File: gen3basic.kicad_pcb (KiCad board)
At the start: 2 copper layers, 35 parts, among them J1 AVR-ISP-6, J2 Screw_Terminal_01x02, J3 Conn_01x08, J4 Conn_01x08, J5 Conn_01x08, J6 Screw_Terminal_01x04, U1 ATMEGA328-PU, Y1 Resonator

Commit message: moved a bunch of stuff around.
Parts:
- removed REF** (x3): MountingHole_2.2mm_M2_DIN965, MountingHole:MountingHole_2.2mm_M2_DIN965
- removed TP1, TP2, TP3: TestPoint, TestPoint:TestPoint_Pad_1.5x1.5mm
- removed TP4: TestPoint, TestPoint:TestPoint_Pad_1.0x1.0mm
- added C4: 100 nF, Capacitor_SMD:C_0805_2012Metric_Pad1.15x1.40mm_HandSolder, F.Cu at (79.2, 49.3)
- added C7: 22pF, Capacitor_SMD:C_0805_2012Metric_Pad1.15x1.40mm_HandSolder, F.Cu at (63.9, 70.0)
- added C8: 22pF, Capacitor_SMD:C_0805_2012Metric_Pad1.15x1.40mm_HandSolder, F.Cu at (59.9, 65.9)
- added D3: 1N4148WS, Diode_SMD:D_SOD-323, F.Cu at (86.4, 53.6)
- added H1: MountingHole, MountingHole:MountingHole_2.2mm_M2_ISO7380, F.Cu at (54.4, 89.9)
- added H2: MountingHole, MountingHole:MountingHole_2.2mm_M2_ISO7380, F.Cu at (78.2, 57.4)
- added H3: MountingHole, MountingHole:MountingHole_2.2mm_M2_ISO7380, F.Cu at (82.3, 80.8)
- added J5: Conn_01x06, Connector_PinHeader_2.54mm:PinHeader_1x06_P2.54mm_Horizontal, F.Cu at (78.1, 46.4)
- added R3: 10k, Resistor_SMD:R_0805_2012Metric_Pad1.15x1.40mm_HandSolder, F.Cu at (87.1, 49.3)
- added R6: 1M, Resistor_SMD:R_0805_2012Metric_Pad1.15x1.40mm_HandSolder, F.Cu at (62.0, 67.9)
- added R7: 330k, Resistor_SMD:R_0805_2012Metric_Pad1.15x1.40mm_HandSolder, F.Cu at (79.5, 69.1)
- added R8: 330k, Resistor_SMD:R_0805_2012Metric_Pad1.15x1.40mm_HandSolder, F.Cu at (84.1, 71.6)
- added S3: MOMENTARY-SWITCH-SPST-SMD-5.2-REDUNDANT, SparkFun-Switches:TACTILE_SWITCH_SMD_5.2MM, F.Cu at (81.3, 75.4)
- added S4: EG1224, Button_Switch_THT:SW_E-Switch_EG1224_SPDT_Angled, F.Cu at (80.0, 88.6)
- C1: footprint Capacitor_SMD:C_1210_3225Metric_Pad1.42x2.65mm_HandSolder -> Capacitor_SMD:C_0805_2012Metric_Pad1.15x1.40mm_HandSolder
- C3: value C -> 100 nF; footprint Capacitor_SMD:C_1210_3225Metric_Pad1.42x2.65mm_HandSolder -> Capacitor_SMD:C_0805_2012Metric_Pad1.15x1.40mm_HandSolder
- C5: renamed from C4; value C -> 100 nF; footprint Capacitor_SMD:C_1210_3225Metric_Pad1.42x2.65mm_HandSolder -> Capacitor_SMD:C_0805_2012Metric_Pad1.15x1.40mm_HandSolder
- D1: footprint LED_SMD:LED_1210_3225Metric_Pad1.42x2.65mm_HandSolder -> LED_THT:LED_D5.0mm_Clear
- D2: footprint LED_SMD:LED_1210_3225Metric_Pad1.42x2.65mm_HandSolder -> LED_SMD:LED_0805_2012Metric_Pad1.15x1.40mm_HandSolder
- D4: renamed from D3; footprint LED_SMD:LED_1210_3225Metric_Pad1.42x2.65mm_HandSolder -> LED_THT:LED_D5.0mm_Clear
- D5: renamed from D4; footprint LED_SMD:LED_1210_3225Metric_Pad1.42x2.65mm_HandSolder -> LED_THT:LED_D5.0mm_Clear
- J3: value Conn_01x08 -> Conn_01x06; footprint Connector_PinHeader_2.54mm:PinHeader_1x08_P2.54mm_Vertical -> Connector_PinHeader_2.54mm:PinHeader_1x06_P2.54mm_Vertical
- J4: value Conn_01x08 -> Conn_01x07; footprint Connector_PinHeader_2.54mm:PinHeader_1x08_P2.54mm_Vertical -> Connector_PinHeader_2.54mm:PinHeader_1x07_P2.54mm_Vertical
- R1: footprint Resistor_SMD:R_1210_3225Metric_Pad1.42x2.65mm_HandSolder -> Resistor_SMD:R_0805_2012Metric_Pad1.15x1.40mm_HandSolder
- R2: footprint Resistor_SMD:R_1210_3225Metric_Pad1.42x2.65mm_HandSolder -> Resistor_SMD:R_1206_3216Metric_Pad1.42x1.75mm_HandSolder
- R4: renamed from R3; footprint Resistor_SMD:R_1210_3225Metric_Pad1.42x2.65mm_HandSolder -> Resistor_SMD:R_1206_3216Metric_Pad1.42x1.75mm_HandSolder
- R5: renamed from R4; footprint Resistor_SMD:R_1210_3225Metric_Pad1.42x2.65mm_HandSolder -> Resistor_SMD:R_1206_3216Metric_Pad1.42x1.75mm_HandSolder
- S1, S2: value 1825910-6 -> MOMENTARY-SWITCH-SPST-SMD-5.2-REDUNDANT; footprint digikey-footprints:Switch_Tactile_THT_6x6mm -> SparkFun-Switches:TACTILE_SWITCH_SMD_5.2MM
- Y1: value Resonator -> 16.0000MHZ 20PF; footprint Crystal:Resonator-3Pin_W10.0mm_H5.0mm -> Crystal:Crystal_HC49-U_Vertical
- moved C6 17.3 mm to (88.9, 53.3)
- moved J1 12.8 mm to (88.3, 59.1)
- moved C2 12.4 mm to (70.1, 83.6)
- moved D2 8.42 mm to (79.8, 84.1)
- moved R1 7.50 mm to (84.3, 84.1)
- moved C1 7.12 mm to (75.4, 84.1)
- moved R2 5.46 mm to (55.6, 83.1)
- moved S2 5.32 mm to (56.1, 57.4)
- moved S1 5.13 mm to (56.1, 49.5)
- moved J4 5.12 mm to (83.2, 51.4)
- moved R5 4.86 mm to (55.6, 79.2)
- moved R4 4.04 mm to (55.6, 75.7)
- moved D4 2.96 mm to (60.2, 76.5)
- moved C3 2.19 mm to (77.0, 65.0)
- moved J3 1.80 mm to (88.3, 69.2)
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- renumbered C5 to C6, D5 to D6, D6 to D7, D7 to D8, J5 to J6, J6 to J7
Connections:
- net /PD0 renamed /PD0-RXD
- net /PD1 renamed /PD1-TXD
- C3 pad 1: GND -> VCC
- C3 pad 2: VCC -> GND
- D6 pad 1: /MISO -> /APA-DI
- D6 pad 2: /PB5 -> /APA-CI
- J1 pad 5: /PC6 -> /RESET#
- J2 pad 1: VCC -> /IN+
- J3 pad 1: GND -> /APA-CI
- J3 pad 2: GND -> /MISO
- J3 pad 3: /PB5 -> /APA-DI
- J3 pad 4: /MISO -> /PB2
- J3 pad 5: /MOSI -> /LED1
- J3 pad 6: /PB2 -> /PB0
- J4 pad 2: /PC6 -> /PC5
- J4 pad 3: /PC5 -> /PC4
- J4 pad 4: /PC4 -> /PC3
- J4 pad 5: /PC3 -> /PC2
- J4 pad 6: /PC2 -> /PC1
- J4 pad 7: /PC1 -> /PC0
- J7 pad 2: /MISO -> /APA-CI
- J7 pad 3: /PB5 -> /APA-DI
- S1 pad 1: VCC -> /PD2
- S1 pad 3: VCC -> GND
- S1 pad 4: /PD2 -> GND
- S2 pad 1: VCC -> /PD3
- S2 pad 3: VCC -> GND
- S2 pad 4: /PD3 -> GND
- U1 pad 1: /PC6 -> /RESET#
- Y1 pad 2: GND -> OSC2
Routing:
- net VCC: track 188.3 -> 78.1 mm, vias 2 -> 1
- net /PB5: track 79.6 -> 20.7 mm
- net /RESET#: track 0.00 -> 41.4 mm, vias 0 -> 1
- net /APA-CI: track 0.00 -> 35.8 mm, vias 0 -> 1
- net /MISO: track 66.8 -> 35.1 mm, vias 1 -> 0
- net /APA-DI: track 0.00 -> 31.2 mm, vias 0 -> 1
- net /PC6: track 22.7 -> 0.00 mm
- net /MOSI: track 45.3 -> 24.2 mm, vias 0 -> 1
- net /PD0-RXD: track 4.86 -> 24.7 mm, vias 0 -> 1
- net /IN+: track 0.00 -> 17.3 mm
- net /PD1-TXD: track 4.86 -> 21.9 mm
- net GND: track 50.7 -> 56.5 mm, vias 4 -> 12
- net Net-(D1-Pad1): track 2.96 -> 8.38 mm
- net /LED2: track 25.5 -> 20.5 mm
- net /PC5: track 9.72 -> 13.5 mm
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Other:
- board outline added: 49.5 x 49.5 mm

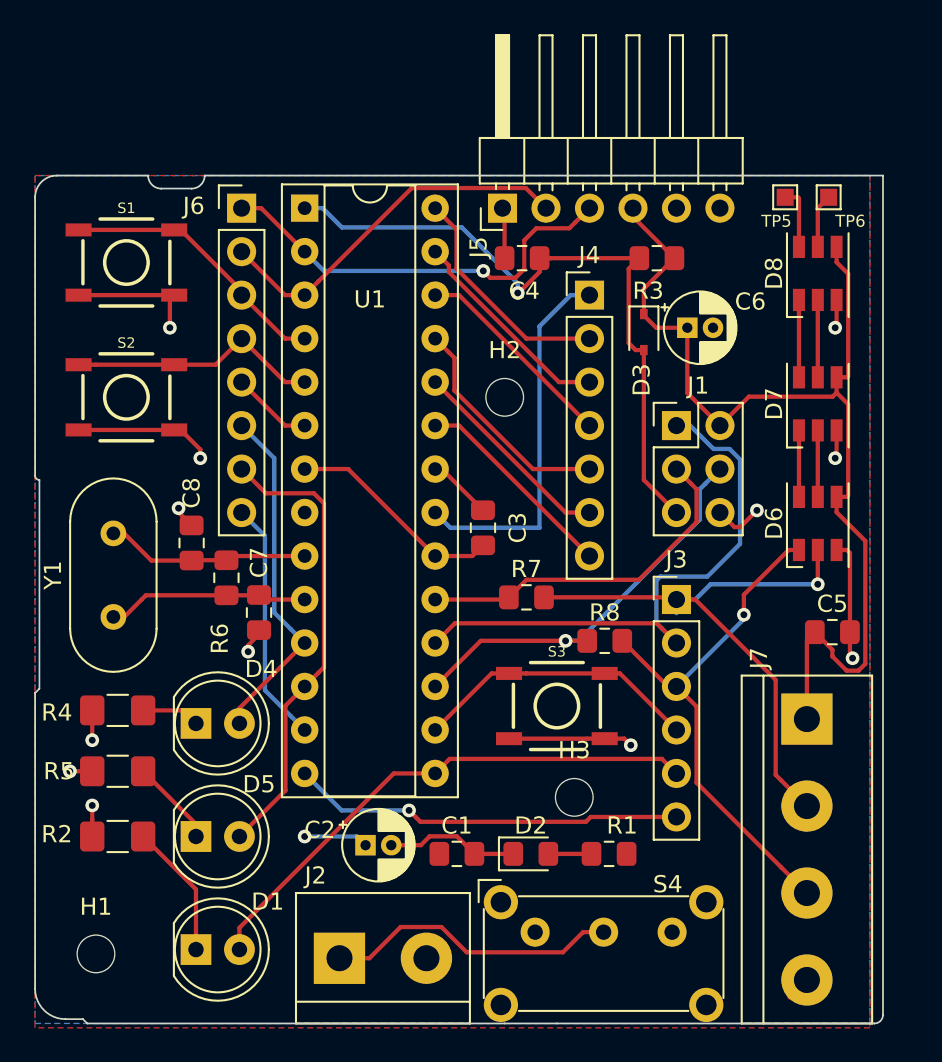
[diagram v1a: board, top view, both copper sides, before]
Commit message: fixing footprints, final design verification, silkscreen.
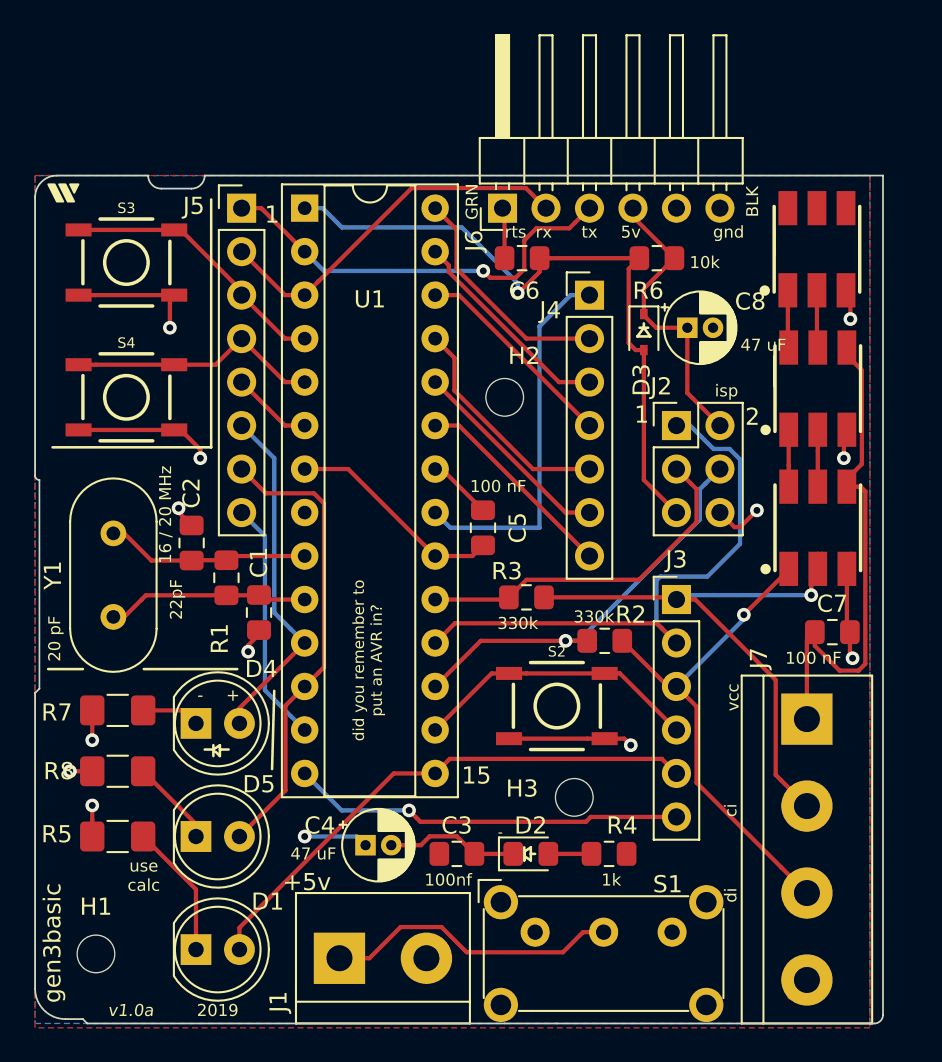
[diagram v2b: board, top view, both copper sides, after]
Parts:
- removed TP5, TP6: TestPoint, TestPoint:TestPoint_Pad_1.0x1.0mm
- added ?: , SparkFun-Aesthetics:OSHW-LOGO-MINI, B.Cu at (98.4, 46.4)
- added G***: LOGO, myFootprints:Linds Fairy, B.Cu at (56.6, 57.8)
- added REF**: W-Logo, myFootprints:W-Logo, B.Cu at (93.6, 52.6)
- D6, D7, D8: value APA102 -> APA102C; footprint LED_SMD:LED_RGB_PLCC-6 -> SparkFun-LED:APA102C
- moved D8 1.41 mm to (96.5, 48.8), turned to 270 degrees
- moved D7 0.89 mm to (96.5, 56.9), turned to 270 degrees
- moved D6 0.25 mm to (96.5, 65.0), turned to 270 degrees
- renumbered C7 to C1, C8 to C2, C1 to C3, C2 to C4, C3 to C5, C4 to C6, C5 to C7, C6 to C8, J2 to J1, J1 to J2, J6 to J5, J5 to J6, R6 to R1, R8 to R2, R7 to R3, R1 to R4, R2 to R5, R3 to R6, R4 to R7, R5 to R8, S4 to S1, S3 to S2, S1 to S3, S2 to S4
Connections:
- net Net-(J4-Pad1) renamed /AREF
- D8 pad 5: Net-(D8-Pad5) -> (no net)
- D8 pad 6: Net-(D8-Pad6) -> (no net)
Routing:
- net VCC: track 78.1 -> 63.9 mm
- net Net-(D8-Pad6): track 3.67 -> 0.00 mm
- net Net-(D8-Pad5): track 3.16 -> 0.00 mm
- net /APA-DI: track 31.2 -> 29.1 mm
- net Net-(D7-Pad6): track 4.52 -> 2.73 mm
- net Net-(D7-Pad5): track 4.52 -> 2.73 mm
- net GND: track 56.5 -> 55.5 mm
- net /APA-CI: track 35.8 -> 35.0 mm
- net Net-(D6-Pad6): track 3.88 -> 3.33 mm
- net Net-(D6-Pad5): track 3.88 -> 3.33 mm
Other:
- board text added: "(Ask He-Man)"
- board text added: "+"
- board text added: "+5v"
- board text added: "-"
- board text added: "1"
- board text added: "100 nF"
- board text added: "100nf"
- board text added: "10k"
- board text added: "15"
- board text added: "16 / 20 MHz"
- board text added: "1k"
- board text added: "2"
- board text added: "20 pF"
- board text added: "2019"
- board text added: "22pF"
- board text added: "28"
- board text added: "330k"
- board text added: "47 uF"
- board text added: "5v"
- board text added: "APA-CI"
- board text added: "APA-DI"
- board text added: "APA102 5050 size goes here"
- board text added: "AREF"
- board text added: "ATMega 8 / 88 / 168 / 328"
- board text added: "ArPin 5"
- board text added: "ArPin 6"
- board text added: "ArPin 9"
- board text added: "BLK"
- board text added: "C1"
- board text added: "C2"
- board text added: "C3"
- board text added: "C5"
- board text added: "Cath(-) = Short Pin = Flat"
- board text added: "Chairs go there"
- board text added: "GND"
- board text added: "GRN"
- board text added: "Good Hole-Some Activity"
- board text added: "LED 1 = PB1"
- board text added: "LED 3 = PD6"
- board text added: "LED2 = PD5"
- board text added: "MISO"
- board text added: "PB0"
- board text added: "PB1"
- board text added: "PB2"
- board text added: "PC0"
- board text added: "PC4"
- board text added: "PD0"
- board text added: "PD1"
- board text added: "PD2"
- board text added: "PD7"
- board text added: "Power"
- board text added: "S3=PD2 ArPin 2"
- board text added: "S4=PD3 ArPin 3"
- board text added: "Serial Connector"
- board text added: "VCC"
- board text added: "ci"
- board text added: "di"
- board text added: "did you remember to put an AVR in?"
- board text added: "gen3basic"
- board text added: "gnd"
- board text added: "isp"
- board text added: "rts"
- board text added: "rx"
- board text added: "s2 = pb2 ArPin 10"
- board text added: "tx"
- board text added: "use calc"
- board text added: "v1.0a"
- board text added: "vcc"
- board text added: "www.wireheadarts.com"

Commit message: update.
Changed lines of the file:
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@@
   )
   (page A4)
+  (title_block
+    (title gen3basic)
+    (date 2019-06-09)
+    (rev v1.0a)
+  )
   (layers
-    (0 F.Cu signal)
-    (31 B.Cu signal)
+    (0 F.Cu signal hide)
+    (31 B.Cu signal hide)
     (32 B.Adhes user hide)
     (33 F.Adhes user hide)
-    (34 B.Paste user)
-    (35 F.Paste user)
+    (34 B.Paste user hide)
+    (35 F.Paste user hide)
     (36 B.SilkS user hide)
     (37 F.SilkS user)
@@
     (pad_drill 0.762)
     (pad_to_mask_clearance 0)
-    (aux_axis_origin 0 0)
+    (aux_axis_origin 50.8 44.45)
     (visible_elements 7FFFFFFF)
     (pcbplotparams
-      (layerselection 0x010fc_ffffffff)
-      (usegerberextensions false)
+      (layerselection 0x00020_7ffffffe)
+      (usegerberextensions true)
       (usegerberattributes false)
       (usegerberadvancedattributes false)
@@
       (viasonmask false)
       (mode 1)
-      (useauxorigin false)
+      (useauxorigin true)
       (hpglpennumber 1)
       (hpglpenspeed 20)
@@
       (outputformat 1)
       (mirror false)
-      (drillshape 1)
+      (drillshape 0)
       (scaleselection 1)
-      (outputdirectory ""))
+      (outputdirectory "gerbers/"))
   )
   (net 0 "")
@@
     (descr "CP, Radial series, Radial, pin pitch=1.50mm, , diameter=4mm, Electrolytic Capacitor")
     (tags "CP Radial series Radial pin pitch 1.50mm  diameter 4mm Electrolytic Capacitor")
-    (fp_text reference C8 (at 3.683 -1.524) (layer F.SilkS)
+    (fp_text reference C8 (at 3.302 -2.159) (layer F.SilkS)
       (effects (font (size 1 1) (thickness 0.15)))
     )
@@
     )
   )
-  (gr_text "47 uF" (at 93.345 54.356) (layer F.SilkS)
+  (gr_text "47 uF" (at 92.202 55.753) (layer F.SilkS)
     (effects (font (size 0.7 0.7) (thickness 0.15)))
   )
